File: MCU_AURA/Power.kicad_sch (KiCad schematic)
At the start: 65 parts, among them J100 XT30PW-M, J101 USB_C_Receptacle_USB2.0_16P, U100 TPS56C230RJER, U101 SI4825DDY-T1-GE3, U102 TPS2115ADRBR, U103 TLV62566DBVR, U104 AP2127N-1.8

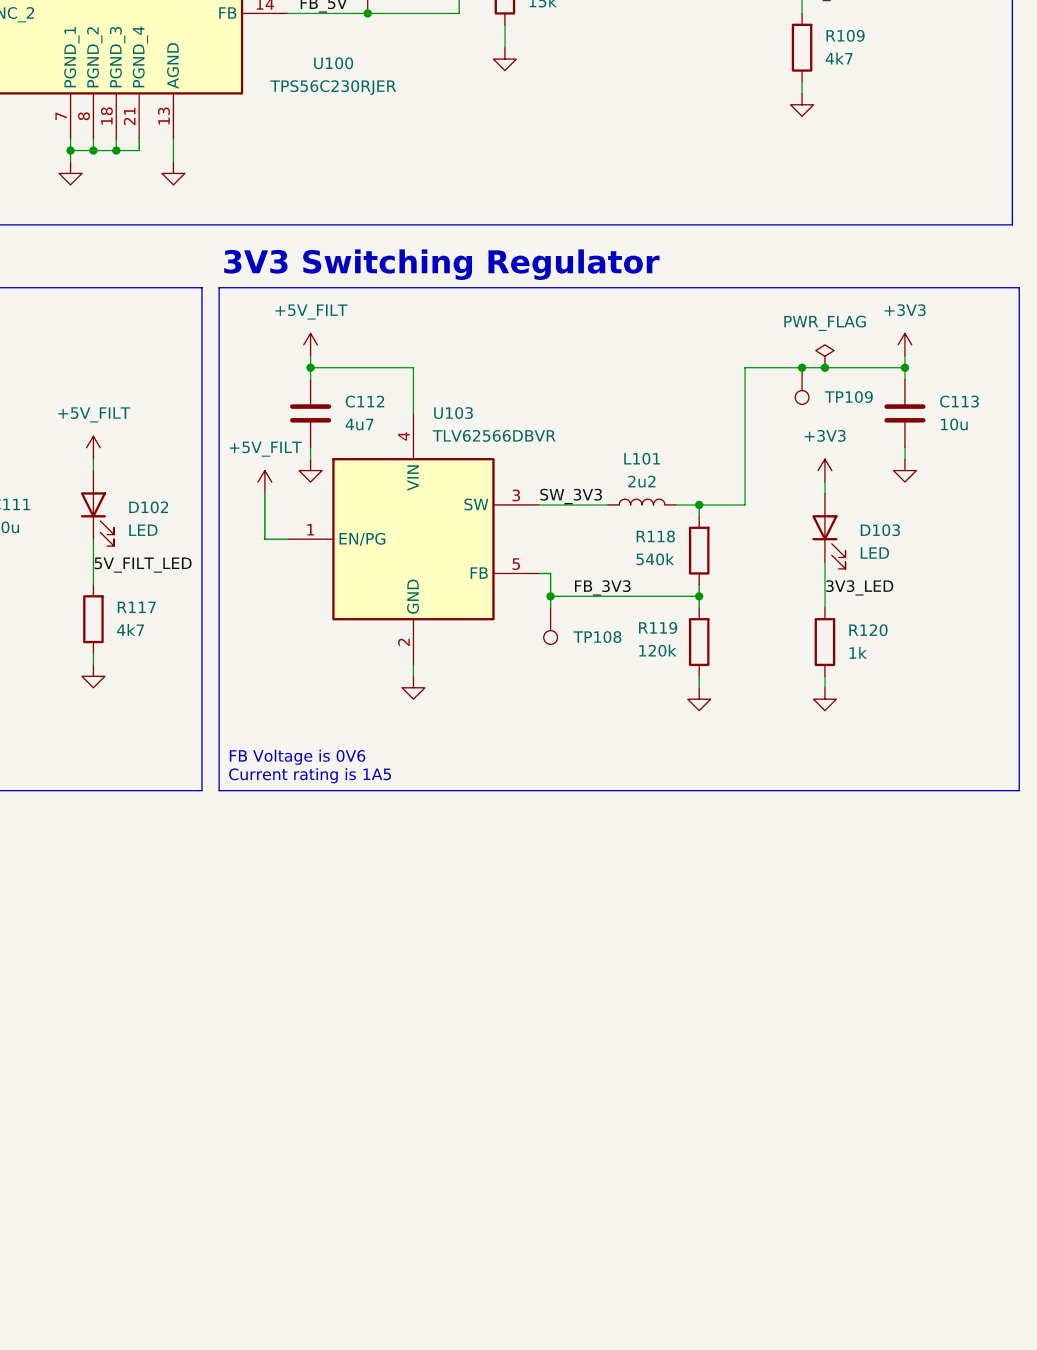
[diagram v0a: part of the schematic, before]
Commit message: Added Samacsys libraries
Made the libraries from the component search engine local.
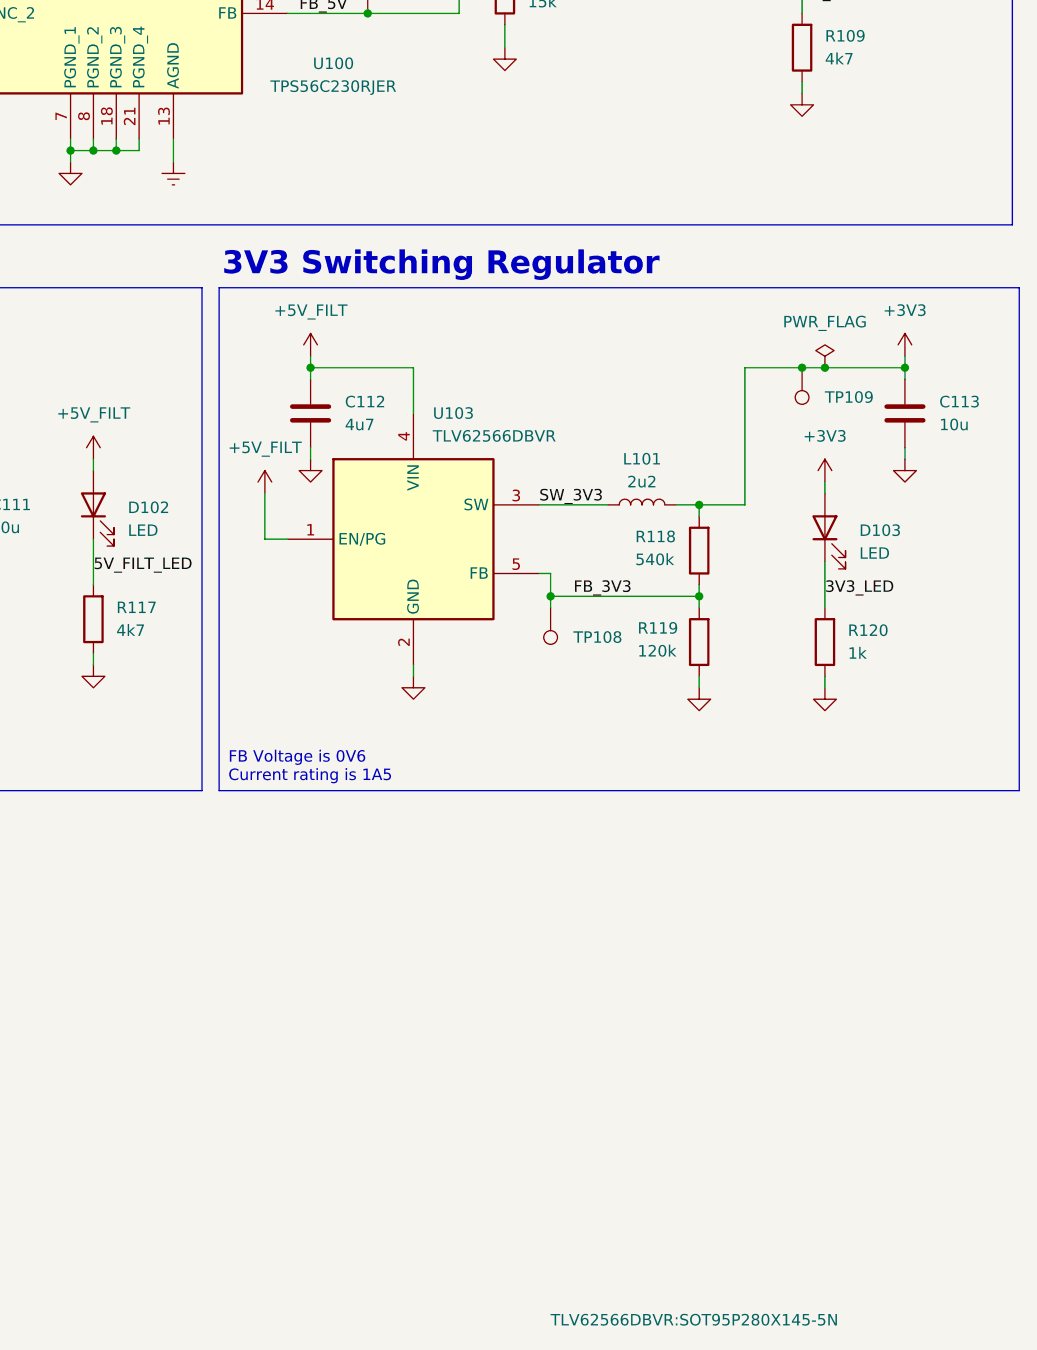
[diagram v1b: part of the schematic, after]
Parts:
- D101: footprint SamacSys_Parts:MMSZ5252B -> MMSZ5252B:MMSZ5252B
- J100: footprint SamacSys_Parts:XT30PWM -> XT30PWM; symbol SamacSys_Parts:XT30PW-M -> XT30PW-M:XT30PW-M
- U100: footprint SamacSys_Parts:QFN45P300X300X100-21N-D -> TPS56C230RJER:QFN45P300X300X100-21N-D
- U102: footprint SamacSys_Parts:SON65P300X300X100-9N-D -> TPS2115ADRBR:SON65P300X300X100-9N-D
- U103: footprint SamacSys_Parts:SOT95P280X145-5N -> TLV62566DBVR:SOT95P280X145-5N
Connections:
- net GND: no longer U100.13 (AGND)
- new net GNDREF: U100.13 (AGND)
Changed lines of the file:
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@@
 			)
 		)
-		(property "Footprint" "SamacSys_Parts:SOT95P280X145-5N"
+		(property "Footprint" "TLV62566DBVR:SOT95P280X145-5N"
 			(at 227.33 215.57 0)
 			(effects
@@
 				)
 				(justify left top)
-				(hide yes)
 			)
 		)
@@
 			)
 		)
-		(property "Footprint" "SamacSys_Parts:QFN45P300X300X100-21N-D"
+		(property "Footprint" "TPS56C230RJER:QFN45P300X300X100-21N-D"
 			(at 186.69 135.56 0)
 			(effects
@@
 	)
 	(symbol
-		(lib_id "SamacSys_Parts:XT30PW-M")
+		(lib_id "XT30PW-M:XT30PW-M")
 		(at 30.48 50.8 0)
 		(unit 1)
@@
 			)
 		)
-		(property "Footprint" "SamacSys_Parts:XT30PWM"
+		(property "Footprint" "XT30PWM"
 			(at 46.99 145.72 0)
 			(effects
@@
 	(symbol
 		(lib_id "power:GND")
-		(at 185.42 87.63 0)
-		(unit 1)
-		(exclude_from_sim no)
-		(in_bom yes)
-		(on_board yes)
-		(dnp no)
-		(fields_autoplaced yes)
-		(property "Reference" "#PWR0137"
-			(at 185.42 93.98 0)
-			(effects
-				(font
-					(size 1.27 1.27)
-				)
-				(hide yes)
-			)
-		)
-		(property "Value" "GND"
-			(at 185.42 92.71 0)
-			(effects
-				(font
-					(size 1.27 1.27)
-				)
-				(hide yes)
-			)
-		)
-		(property "Footprint" ""
-			(at 185.42 87.63 0)
-			(effects
-				(font
-					(size 1.27 1.27)
-				)
-				(hide yes)
-			)
-		)
-		(property "Datasheet" ""
-			(at 185.42 87.63 0)
-			(effects
-				(font
-					(size 1.27 1.27)
-				)
-				(hide yes)
-			)
-		)
-		(property "Description" "Power symbol creates a global label with name \"GND\" , ground"
-			(at 185.42 87.63 0)
-			(effects
-				(font
-					(size 1.27 1.27)
-				)
-				(hide yes)
-			)
-		)
-		(pin "1"
-		)
-		(instances
-			(project "Summer2025"
-				(path "/c0b09de1-c640-438f-9ef5-dda14a6aac71/c5906580-2f17-4557-899f-eb3151fe9c9e"
-					(reference "#PWR0137")
-					(unit 1)
-				)
-			)
-		)
-	)
-	(symbol
-		(lib_id "power:GND")
 		(at 201.93 41.91 0)
 		(unit 1)
@@
 			)
 		)
-		(property "Footprint" "SamacSys_Parts:MMSZ5252B"
+		(property "Footprint" "MMSZ5252B:MMSZ5252B"
 			(at -35.23 129.54 0)
 			(effects
@@
 	)
 	(symbol
+		(lib_id "power:GNDREF")
+		(at 185.42 87.63 0)
+		(unit 1)
+		(exclude_from_sim no)
+		(in_bom yes)
+		(on_board yes)
+		(dnp no)
+		(fields_autoplaced yes)
+		(property "Reference" "#PWR01"
+			(at 185.42 93.98 0)
+			(effects
+				(font
+					(size 1.27 1.27)
+				)
+				(hide yes)
+			)
+		)
+		(property "Value" "GNDREF"
+			(at 185.42 92.71 0)
+			(effects
+				(font
+					(size 1.27 1.27)
+				)
+				(hide yes)
+			)
+		)
+		(property "Footprint" ""
+			(at 185.42 87.63 0)
+			(effects
+				(font
+					(size 1.27 1.27)
+				)
+				(hide yes)
+			)
+		)
+		(property "Datasheet" ""
+			(at 185.42 87.63 0)
+			(effects
+				(font
+					(size 1.27 1.27)
+				)
+				(hide yes)
+			)
+		)
+		(property "Description" "Power symbol creates a global label with name \"GNDREF\" , reference supply ground"
+			(at 185.42 87.63 0)
+			(effects
+				(font
+					(size 1.27 1.27)
+				)
+				(hide yes)
+			)
+		)
+		(pin "1"
+		)
+		(instances
+			(project ""
+				(path "/c0b09de1-c640-438f-9ef5-dda14a6aac71/c5906580-2f17-4557-899f-eb3151fe9c9e"
+					(reference "#PWR01")
+					(unit 1)
+				)
+			)
+		)
+	)
+	(symbol
 		(lib_id "power:GND")
 		(at 27.94 186.69 0)
@@
 			)
 		)
-		(property "Footprint" "SamacSys_Parts:SON65P300X300X100-9N-D"
+		(property "Footprint" "TPS2115ADRBR:SON65P300X300X100-9N-D"
 			(at 146.05 216.84 0)
 			(effects

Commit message: Synchronised
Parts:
- removed D101: MMSZ5242B, MMSZ5252B:MMSZ5252B, symbol SamacSys_Parts:MMSZ5242B
- removed J100: XT30PW-M, XT30PWM, symbol XT30PW-M:XT30PW-M
- removed U100: TPS56C230RJER, TPS56C230RJER:QFN45P300X300X100-21N-D, symbol SamacSys_Parts:TPS56C230RJER
- removed U102: TPS2115ADRBR, TPS2115ADRBR:SON65P300X300X100-9N-D, symbol SamacSys_Parts:TPS2115ADRBR
- removed U103: TLV62566DBVR, TLV62566DBVR:SOT95P280X145-5N, symbol SamacSys_Parts:TLV62566DBVR
- added D1: MMSZ5242B, MMSZ5252B:MMSZ5252B, symbol MMSZ5252B:MMSZ5242B
- added J3: XT30PW-M, XT30PWM:XT30PWM, symbol XT30PW-M:XT30PW-M
- added U2: TPS56C230RJER, TPS56C230RJER:QFN45P300X300X100-21N-D, symbol TPS56C230RJER:TPS56C230RJER
- added U3: TPS2115ADRBR, TPS2115ADRBR:SON65P300X300X100-9N-D, symbol TPS2115ADRBR:TPS2115ADRBR
- added U4: TLV62566DBVR, TLV62566DBVR:SOT95P280X145-5N, symbol TLV62566DBVR:TLV62566DBVR
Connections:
- net +5V: now also U3.6 (IN2)
- net +5V_FILT: now also U3.7 (OUT), U4.1 (EN/PG), U4.4 (VIN)
- net +BATT: now also J3.1
- net +BATT_FILT: now also D1.1 (K), U2.2 (VIN_1), U2.3 (VIN_2), U2.4 (VIN_3), U2.5 (VIN_4)
- net +VUSB: now also U3.3 (D1), U3.8 (IN1)
- net BST_5V: now also U2.1 (BST)
- net EN_5V: now also U2.12 (EN)
- net FB_3V3: now also U4.5 (FB)
- net FB_5V: now also U2.14 (FB)
- net GND: now also J3.2, J3.3, J3.4, U2.10 (NC_1), U2.16 (NC_2), U2.18 (PGND_3), U2.21 (PGND_4), U2.7 (PGND_1), U2.8 (PGND_2), U3.2 (D0), U3.5 (GND_1), U3.9 (GND_2), U4.2 (GND)
- net GNDREF: now also U2.13 (AGND)
- net MODE: now also U2.15 (MODE)
- net PGOOD: now also U2.9 (PGOOD)
- net SS_5V: now also U2.11 (SS)
- net SW_3V3: now also U4.3 (SW)
- net SW_5V: now also U2.19 (SW_2), U2.20 (SW_3), U2.6 (SW_1)
- net VCC: now also U2.17 (VCC)
- net rvrs_plr: now also D1.2 (A)
- net at R116.2: now also U3.4 (ILIM)
- net at TP107.1: now also U3.1 (STAT)

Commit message: Adding Connectors
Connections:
- net STAT_5V_SW: now reaches TP107.1, U3.1 (STAT)
- net ILIM_5V_SW: now reaches R116.2, U3.4 (ILIM)
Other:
- moved on the sheet: TP107
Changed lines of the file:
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@@
 	(wire
 		(pts
-			(xy 146.05 130.81) (xy 147.32 130.81)
-		)
-		(stroke
-			(width 0)
-			(type default)
-		)
-	)
-	(wire
-		(pts
 			(xy 185.42 85.09) (xy 185.42 87.63)
 		)
@@
 	(wire
 		(pts
+			(xy 156.21 130.81) (xy 156.21 132.08)
+		)
+		(stroke
+			(width 0)
+			(type default)
+		)
+	)
+	(wire
+		(pts
 			(xy 227.33 137.16) (xy 227.33 135.89)
 		)
@@
 	(wire
 		(pts
+			(xy 146.05 130.81) (xy 156.21 130.81)
+		)
+		(stroke
+			(width 0)
+			(type default)
+		)
+	)
+	(wire
+		(pts
 			(xy 43.18 116.84) (xy 44.45 116.84)
 		)
@@
 		)
 	)
+	(label "STAT_5V_SW"
+		(at 146.05 130.81 0)
+		(effects
+			(font
+				(size 1.27 1.27)
+			)
+			(justify left bottom)
+		)
+	)
 	(label "CC2"
 		(at 90.17 45.72 0)
@@
 		)
 	)
+	(label "ILIM_5V_SW"
+		(at 102.87 129.54 0)
+		(effects
+			(font
+				(size 1.27 1.27)
+			)
+			(justify left bottom)
+		)
+	)
 	(label "PGOOD"
 		(at 149.86 55.88 0)
@@
 	(symbol
 		(lib_id "Connector:TestPoint")
-		(at 147.32 130.81 270)
+		(at 156.21 132.08 180)
 		(unit 1)
 		(exclude_from_sim no)
@@
 		(on_board yes)
 		(dnp no)
-		(fields_autoplaced yes)
 		(property "Reference" "TP107"
-			(at 152.4 130.8099 90)
+			(at 149.606 133.604 0)
 			(effects
 				(font
 					(size 1.27 1.27)
 				)
-				(justify left)
+				(justify right)
 			)
 		)
 		(property "Value" "TestPoint"
-			(at 149.3521 133.35 0)
+			(at 153.67 134.1121 0)
 			(effects
 				(font
@@
 		)
 		(property "Footprint" "TestPoint:TestPoint_Pad_D1.0mm"
-			(at 147.32 135.89 0)
+			(at 151.13 132.08 0)
 			(effects
 				(font
@@
 		)
 		(property "Datasheet" "~"
-			(at 147.32 135.89 0)
+			(at 151.13 132.08 0)
 			(effects
 				(font
@@
 		)
 		(property "Description" "test point"
-			(at 147.32 130.81 0)
+			(at 156.21 132.08 0)
 			(effects
 				(font
@@
 		(on_board yes)
 		(dnp no)
-		(fields_autoplaced yes)
 		(property "Reference" "U2"
-			(at 201.93 46.9198 0)
+			(at 203.2 75.946 0)
 			(effects
 				(font
@@
 		)
 		(property "Value" "TPS56C230RJER"
-			(at 201.93 49.4598 0)
+			(at 203.2 78.486 0)
 			(effects
 				(font

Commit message: Initial Schematic Draft
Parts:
- removed C100: 1u, Capacitor_SMD:C_0402_1005Metric, symbol Device:C
- removed C101, C102: 22u, Capacitor_SMD:C_1206_3216Metric, symbol Device:C
- removed C103: 18n, Capacitor_SMD:C_0402_1005Metric, symbol Device:C
- removed C104: 100n, Capacitor_SMD:C_0402_1005Metric, symbol Device:C
- removed C105: 100n, Capacitor_SMD:C_0603_1608Metric, symbol Device:C
- removed C106, C107, C108: 22u, Capacitor_SMD:C_0805_2012Metric, symbol Device:C
- removed D1: MMSZ5242B, MMSZ5252B:MMSZ5252B, symbol MMSZ5252B:MMSZ5242B
- removed D100: LED, LED_SMD:LED_0603_1608Metric, symbol Device:LED
- removed J3: XT30PW-M, XT30PWM:XT30PWM, symbol XT30PW-M:XT30PW-M
- removed L100: 1u8, CKST0603:CKST0603-1.5uHM, symbol Device:L_Iron
- removed R102: 49k, Resistor_SMD:R_0402_1005Metric, symbol Device:R
- removed R103: 13k, Resistor_SMD:R_0402_1005Metric, symbol Device:R
- removed R104: 180k, Resistor_SMD:R_0402_1005Metric, symbol Device:R
- removed R105: 33k, Resistor_SMD:R_0402_1005Metric, symbol Device:R
- removed R106: 330k, Resistor_SMD:R_0402_1005Metric, symbol Device:R
- removed R107: 110k, Resistor_SMD:R_0402_1005Metric, symbol Device:R
- removed R108: 15k, Resistor_SMD:R_0402_1005Metric, symbol Device:R
- removed R109: 4k7, Resistor_SMD:R_0402_1005Metric, symbol Device:R
- removed R110: 100k, Resistor_SMD:R_0402_1005Metric, symbol Device:R
- removed R111: 220k, Resistor_SMD:R_0402_1005Metric, symbol Device:R
- removed R112: 22k, Resistor_SMD:R_0402_1005Metric, symbol Device:R
- removed TP101, TP102, TP103, TP104, TP105: TestPoint, TestPoint:TestPoint_Pad_D1.0mm, symbol Connector:TestPoint
- removed U101: SI4825DDY-T1-GE3, SI4825DDY-T1-GE3:SI4825DDY-T1-GE3, symbol SI4825DDY-T1-GE3:SI4825DDY-T1-GE3
- removed U2: TPS56C230RJER, TPS56C230RJER:QFN45P300X300X100-21N-D, symbol TPS56C230RJER:TPS56C230RJER
- renumbered C109 to C100, C110 to C101, C111 to C102, C112 to C103, C113 to C104, C114 to C105, C115 to C106, D102 to D100, J101 to J100, R116 to R102, R115 to R103, R117 to R104, R118 to R105, R119 to R106, R120 to R107, TP106 to TP101, TP107 to TP102, TP108 to TP103, TP109 to TP104, TP110 to TP105, U3 to U100, U4 to U101, U104 to U102
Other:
- note added: "Shield grounded by host"
- note added: "USB"
- note removed: "5V Switching Regulator"
- note removed: "Current rating is 12A FB Voltage is 0V6 EN is high when > 1V35 => BATT_FLIT > 6V5 Switching frequency is 500kHz Mode is FCCM for constant switching freq"
- note removed: "Reverse polarity protection"
- note removed: "Shield grounded by host Expected input 7V2 to 16V8"
- note removed: "USB and battery"
- moved on the sheet: C100, C101, C102, C103, C104, C105, C106, D100, D103, H1, H2, H3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

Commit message: Started Routing
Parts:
- added C100: 10u, Capacitor_SMD:C_0402_1005Metric, symbol Device:C
- added C101: 1u, Capacitor_SMD:C_0402_1005Metric, symbol Device:C
- added C102: 100n, Capacitor_SMD:C_0402_1005Metric, symbol Device:C
- added D100, D101, D102: TPD1E05U06DPYR, TPD1E05U06DPYR:DIO_TPD1E05U06DPYR, symbol ESDALC5_1BM2:ESDALC5-1BM2
- added R105, R109: 10k, Resistor_SMD:R_0402_1005Metric, symbol Device:R
- added TP105: TestPoint, TestPoint:TestPoint_Pad_D1.0mm, symbol Connector:TestPoint
- H1, H2, H3, H4: footprint MountingHole:MountingHole_4mm_Pad_Via -> MountingHole:MountingHole_3.2mm_M3_Pad_Via
- R102: value 680R -> 270R
- R103: value 220k -> 10k
- R106: renamed from R105; value 540k -> 68k
- R107: renamed from R106; value 120k -> 15k
- renumbered C100 to C103, C101 to C104, C102 to C105, C103 to C106, C104 to C107, C105 to C108, C106 to C109, D100 to D103, D103 to D104, R107 to R108, TP105 to TP106
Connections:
- net +3V3: now also R105.2, R109.2
- net +5V_FILT: no longer U101.1 (EN/PG)
- net +VUSB: now also C100.1, C101.1, C102.1, D102.1
- net CC1: now also R101.2, D101.1; no longer R100.2
- net CC2: now also R100.2, D100.1; no longer R101.2
- net GND: now also C100.2, C101.2, C102.2, D100.2, D101.2, D102.2
- net STAT_5V_SW: now also R105.1
- net ILIM_5V_SW renamed ILIM_5V
- new net PG_3V3: R109.1, TP105.1, U101.1 (EN/PG)
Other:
- note added: "FB Voltage is 0V6 Current rating is 1A5 Resistors must be 1% EN/PG is PG on TLV62566 variant"
- note added: "Use USB power if available for MCU Current limit is set to 1A85 Solder-bridge in case this does not work"
- note removed: "FB Voltage is 0V6 Current rating is 1A5"
- note removed: "Use USB power if available for MCU Current rating is 2A Solder-bridge in case this does not work"
- moved on the sheet: C103, C104, C105, C106, C107, C108, C109, D103, D104, J100, JP100, JP101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

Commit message: First fully routed version
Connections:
- net GND: now also H1.1, H2.1, H3.1, H4.1
- no-connect marks 7 -> 3

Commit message: First version
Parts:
- J100: footprint Connector_USB:USB_C_Receptacle_GCT_USB4105-xx-A_16P_TopMnt_Horizontal -> USB-C:USB_C_Receptacle_GCT_USB4105-xx-A_16P_TopMnt_Horizontal
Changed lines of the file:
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@@
 			)
 		)
-		(property "Footprint" "Connector_USB:USB_C_Receptacle_GCT_USB4105-xx-A_16P_TopMnt_Horizontal"
+		(property "Footprint" "USB-C:USB_C_Receptacle_GCT_USB4105-xx-A_16P_TopMnt_Horizontal"
 			(at 45.72 57.15 0)
 			(effects

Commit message: Second Iteration
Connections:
- no-connect marks 3 -> 2
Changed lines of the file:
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@@
 	)
 	(no_connect
-		(at 34.29 80.01)
-	)
-	(no_connect
 		(at 57.15 69.85)
 	)
@@
 		(pin "A7"
 		)
-		(pin "S1"
-		)
 		(pin "A1"
